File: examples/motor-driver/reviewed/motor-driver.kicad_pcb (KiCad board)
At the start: 2 copper layers, 88 x 50 mm, 12 parts, among them J1 VM 2.7-10.8V, J2 MOTOR A, J3 MOTOR B, J4 LOGIC, U1 DRV8833PW

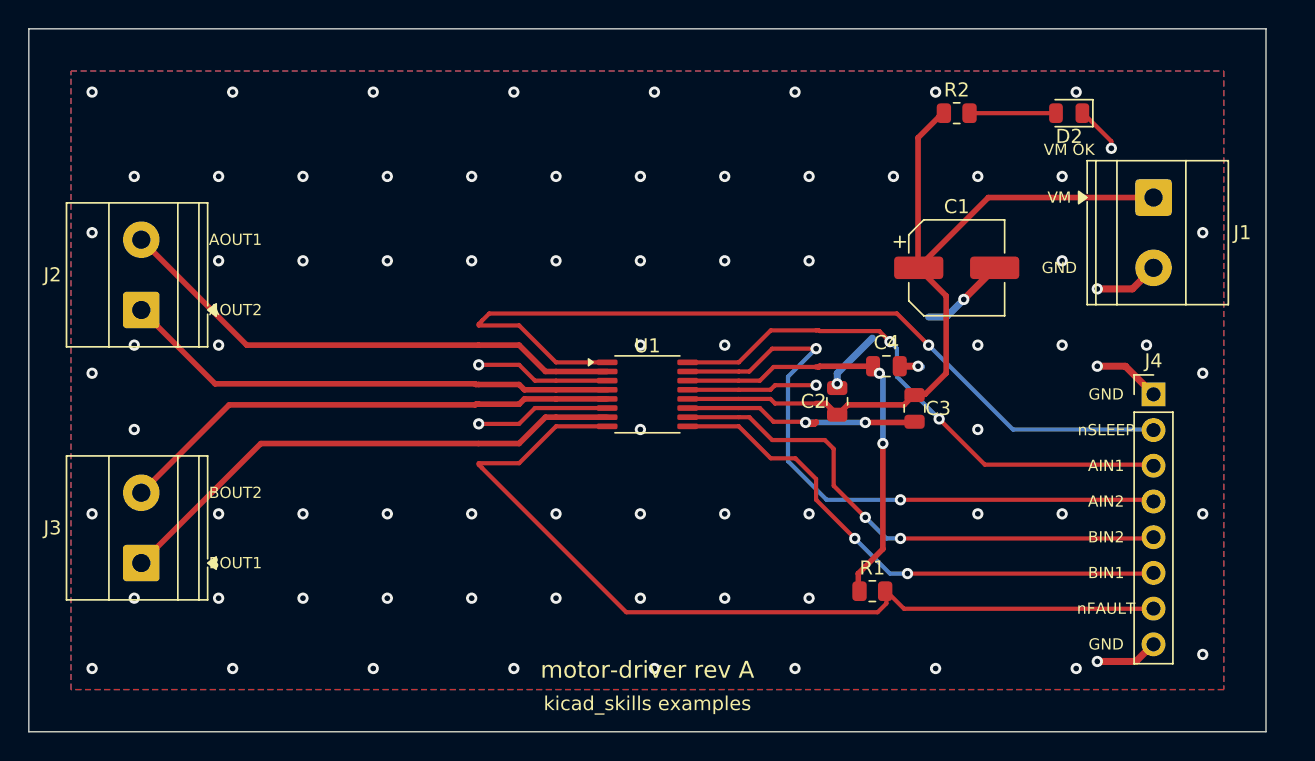
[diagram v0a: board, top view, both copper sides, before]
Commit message: Give the motor board a floorplan its signals can be routed on
The right hand third was a horseshoe: four logic signals leaving the
package on the east side went up over the top of the board, round the
outside and back into the header from behind - 190 mm of copper for a
40 mm net, and four short back-layer runs each cutting the plane under
the track that fed it. The router was not being stupid. The corridor
between the package and the header was walled off by the VM chain
running from the bulk cap down to the charge pump, and going round was
the only way through.

So the floorplan says what it means now. The header sits where the fan
lands, pin for pin and in the same order, so the four inputs run
straight across. The three small caps sit in the middle band with the
supply pins that own them, and the logic passes above and below them.
The bulk cap and the input terminal are at the top edge, out of the way.

That leaves VM needing to reach the middle of a row the logic leaves
from either side of. On two layers something has to cross, and the
choice is which: four signals going round the world, or one stated link
on the back for the rail. The rail is the right answer - it is low
impedance, the plane it crosses is its own return, and the signals cross
the cut it leaves at right angles, a track width each rather than a
detour. It is in the file as a link, not as something a search stumbled
into.

Ground leaves the fan and takes one more step before dropping into the
plane, because on top of a 0.65 mm escape the pour is whatever fits
between two lanes - a strip too thin to reach anything. Stitching vias
now ask for the same thing: a clearance plus a sliver's worth of copper
to hold on to, rather than the clearance alone.

route.return_path 4 -> 0, route.detour 1 -> 0, route.acute_angle 1 -> 0,
layout.pour_fragmented 1 -> 0, track.thin_power and route.width_step to
zero. The zone-island DRC errors are older than this change and still
there; they are the fill's own problem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
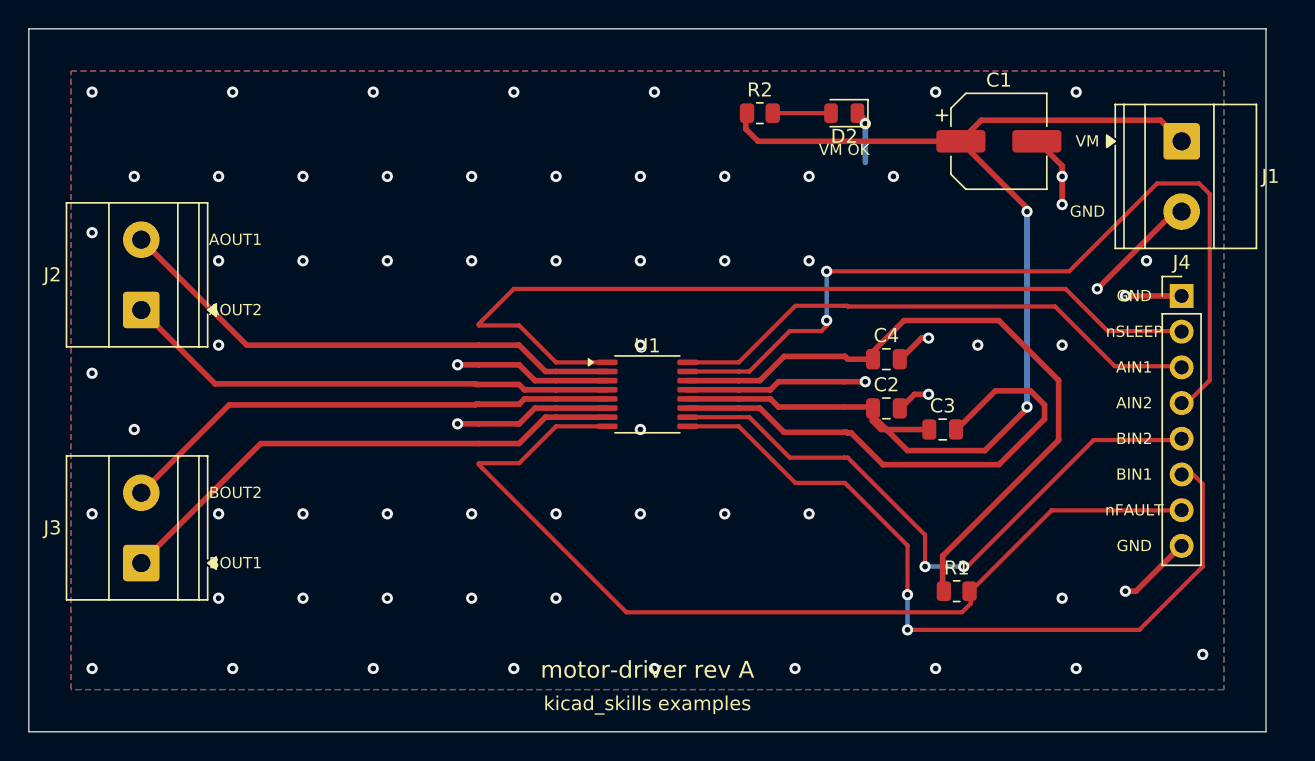
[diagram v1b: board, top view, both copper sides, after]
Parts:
- moved D2 16.0 mm to (158.0, 66.0)
- moved R2 14.0 mm to (152.0, 66.0)
- moved C1 9.49 mm to (169.0, 68.0)
- moved J4 7.28 mm to (182.0, 79.0)
- moved R1 6.00 mm to (166.0, 100.0)
- moved J1 4.47 mm to (182.0, 68.0)
- moved C2 3.54 mm to (161.0, 87.0), turned to 0 degrees
- moved C3 2.50 mm to (165.0, 88.5), turned to 0 degrees
- moved C4 0.50 mm to (161.0, 83.5)
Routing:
- net /VM: track 59.0 -> 87.2 mm, vias 0 -> 2
- net /VCP: track 18.2 -> 37.3 mm, vias 2 -> 0
- net /VINT: track 30.7 -> 48.9 mm, vias 2 -> 0
- net /BIN1: track 38.4 -> 55.7 mm
- net /AIN2: track 45.8 -> 61.2 mm
- net GND: track 58.2 -> 66.9 mm, vias 83 -> 69
- net /BIN2: track 38.3 -> 44.6 mm
- net /nFAULT: track 64.5 -> 68.3 mm
- net /LED_A: track 6.15 -> 4.15 mm
- net /AIN1: track 39.2 -> 38.6 mm, vias 2 -> 0
- net /nSLEEP: track 62.1 -> 62.6 mm, vias 1 -> 0
